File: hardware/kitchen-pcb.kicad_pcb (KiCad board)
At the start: 2 copper layers, 91.6 x 88 mm, 78 parts, among them IC1 ESP32-S3-WROOM-1-N8R8, J1 GSD090012SEU, J2 Conn_02x02_Odd_Even, J3 Conn_01x06, J4 Conn_01x03, J5 DCJ200-10-A-K1-K, J6 USB4105-GF-A, Q1 TEMT6000X01, SW1 SW_Push, SW2 SW_Push, U1 SHT30-DIS-B, U2 MX25L3233FM2I-08G, U3 NCP1117ST33T3G, U4 USBLC6-2SC6

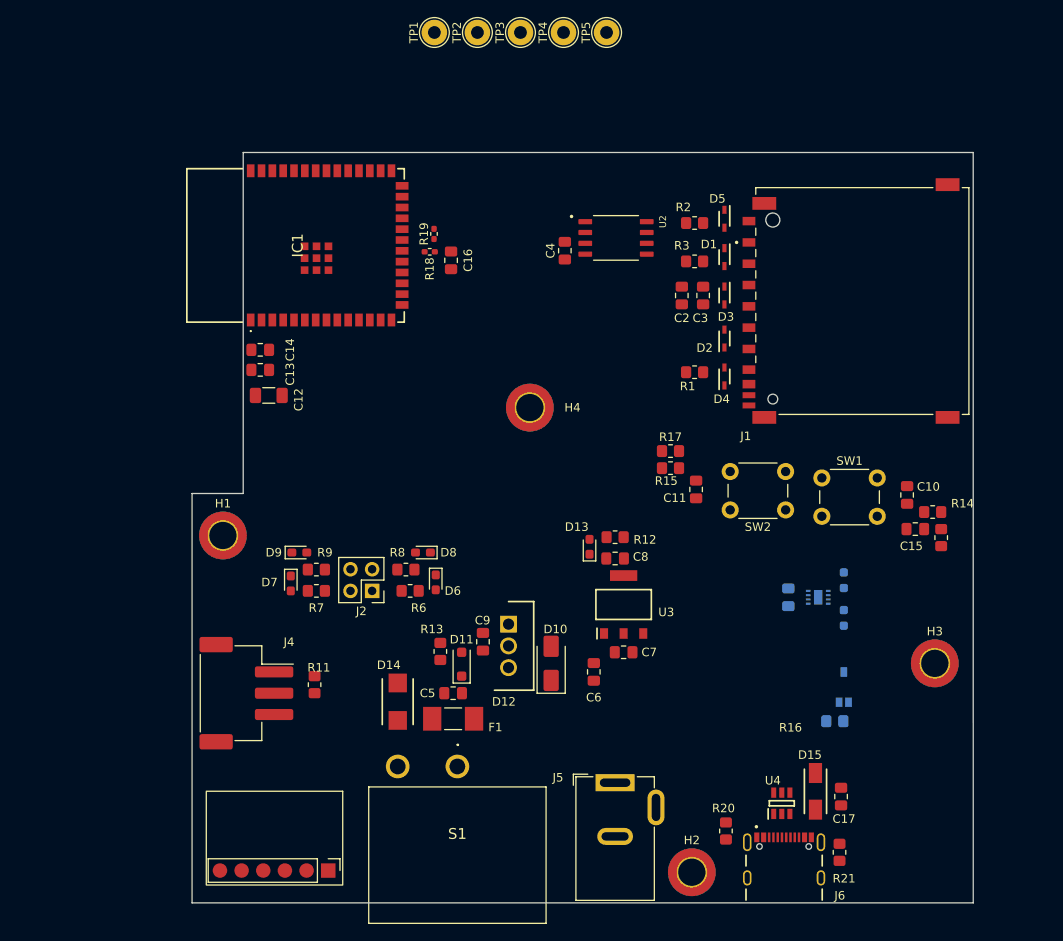
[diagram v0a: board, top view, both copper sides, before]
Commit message: Schematics adjustments - updated some components
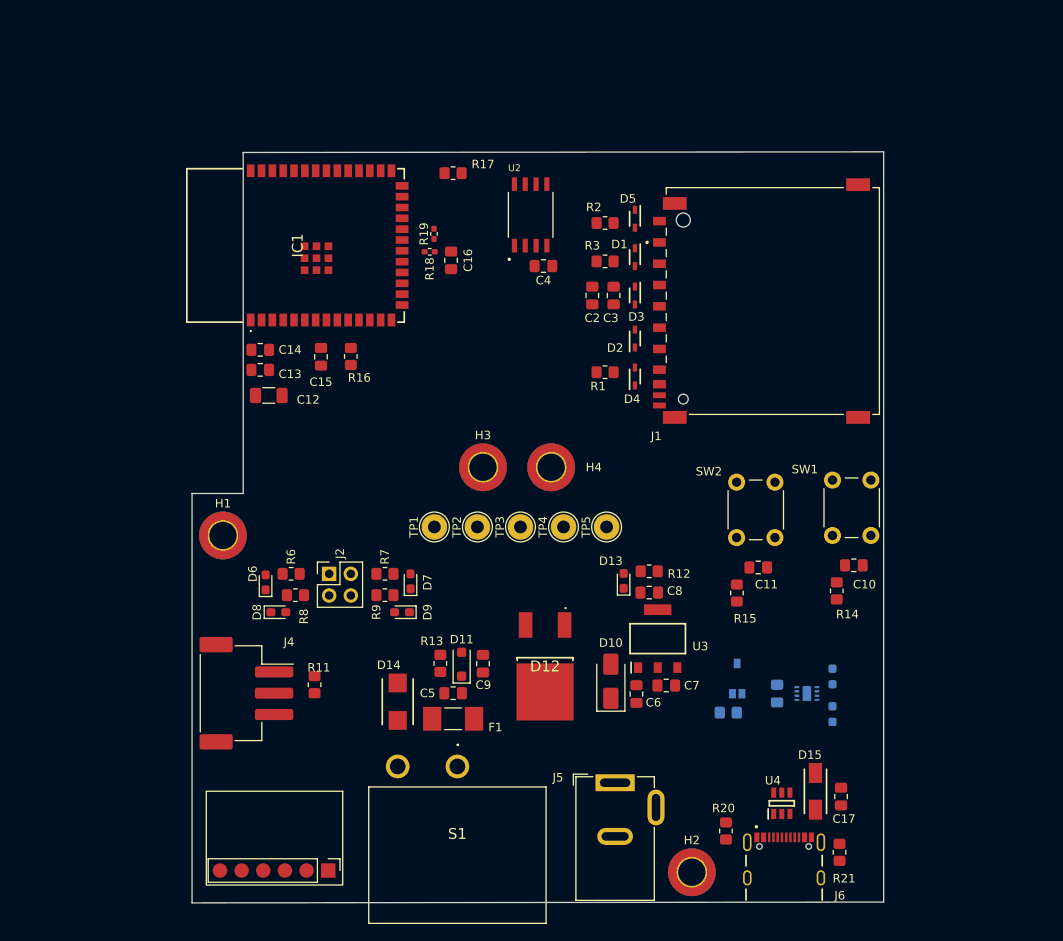
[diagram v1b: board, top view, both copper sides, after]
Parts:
- D11: value NZH6V2B,115 -> NZH5V6B,115
- D12: footprint ESP32-project-footprints:TO255P460X1020X2005-3P -> ESP32-project-footprints:TS820600B
- moved C15 72.6 mm to (112.5, 82.5), turned to 90 degrees
- moved R16 72.4 mm to (116.0, 82.5)
- moved TP1 58.0 mm to (125.8, 102.5)
- moved TP2 58.0 mm to (130.8, 102.5)
- moved TP3 58.0 mm to (135.9, 102.5)
- moved TP4 58.0 mm to (140.9, 102.5)
- moved TP5 58.0 mm to (146.0, 102.5)
- moved H3 57.8 mm to (131.5, 95.5)
- moved R17 41.4 mm to (128.0, 61.0)
- moved D6 20.0 mm to (106.0, 109.0), turned to 90 degrees
- moved D8 18.3 mm to (107.5, 112.5), turned to 0 degrees
- moved R15 16.6 mm to (161.3, 110.2), turned to -90 degrees
- moved R14 14.6 mm to (173.0, 110.0), turned to -90 degrees
- moved R6 14.1 mm to (109.0, 108.0), turned to 180 degrees
- moved D7 14.0 mm to (123.0, 108.9), turned to 90 degrees
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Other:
- board size 91.6 x 88 mm -> 81.1 x 88.1 mm

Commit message: Added notes to schematics, SPI modifications
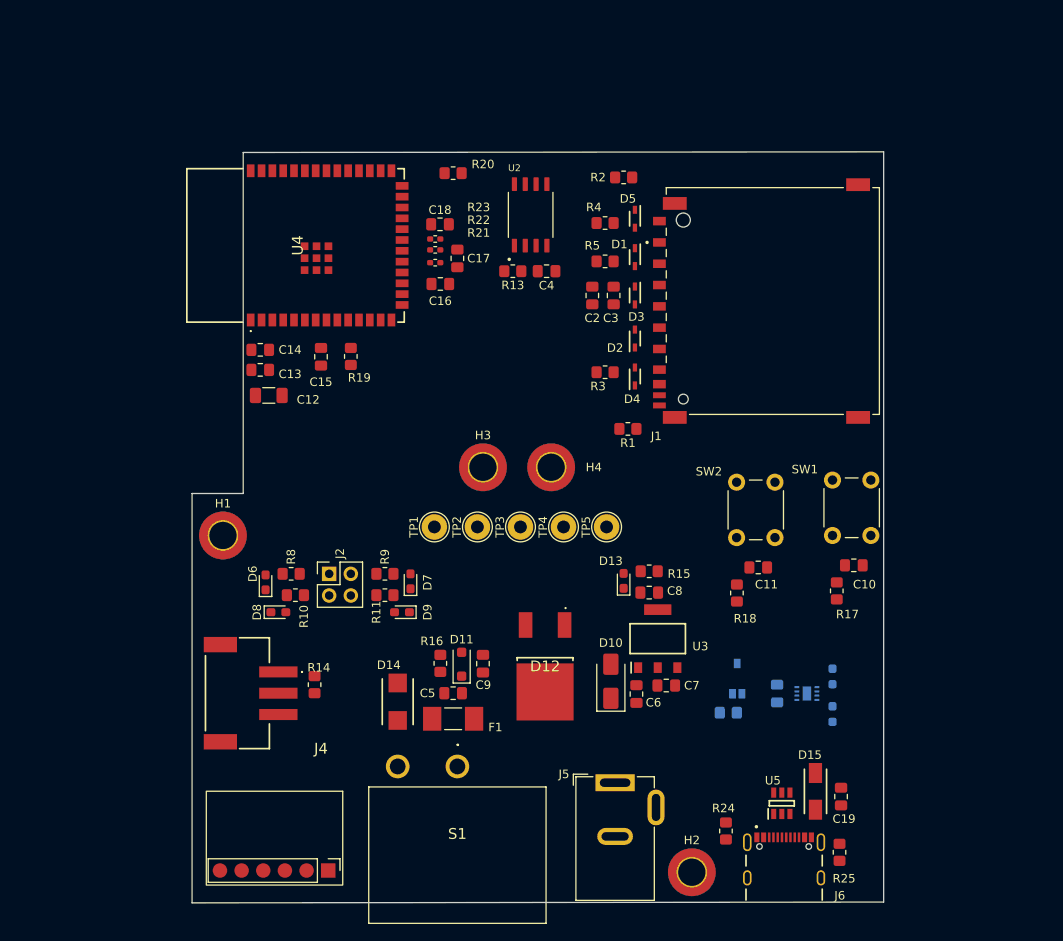
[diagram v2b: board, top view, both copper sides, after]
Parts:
- added C16: 22p, Capacitor_SMD:C_0805_2012Metric_Pad1.18x1.45mm_HandSolder, F.Cu at (126.5, 74.0)
- added C18: 22p, Capacitor_SMD:C_0805_2012Metric_Pad1.18x1.45mm_HandSolder, F.Cu at (126.5, 67.0)
- added R1: 10k, Resistor_SMD:R_0805_2012Metric_Pad1.20x1.40mm_HandSolder, F.Cu at (148.5, 91.0)
- added R13: 10k, Resistor_SMD:R_0805_2012Metric_Pad1.20x1.40mm_HandSolder, F.Cu at (135.0, 72.5)
- added R2: 10k, Resistor_SMD:R_0805_2012Metric_Pad1.20x1.40mm_HandSolder, F.Cu at (148.0, 61.5)
- added R21: 50R, Resistor_SMD:R_0402_1005Metric_Pad0.72x0.64mm_HandSolder, F.Cu at (125.9, 71.5)
- C17: renamed from C16; value 100n -> 22p
- J4: value Conn_01x03 -> S3B-XH-SM4-TB_LF__SN_; footprint Connector_JST:JST_XH_S3B-XH-SM4-TB_1x03-1MP_P2.50mm_Horizontal -> ESP32-project-footprints:S3BXHSM4TBLFSN
- moved C17 0.78 mm to (128.5, 71.0)
- moved C4 0.71 mm to (139.0, 72.5)
- moved R22 0.68 mm to (125.9, 70.0)
- moved R23 0.61 mm to (125.9, 68.7), turned to 0 degrees
- moved J4 0.53 mm to (103.2, 122.0), turned to 90 degrees
- renumbered C17 to C19, R8 to R10, R9 to R11, R10 to R12, R11 to R14, R12 to R15, R13 to R16, R14 to R17, R15 to R18, R16 to R19, R17 to R20, R18 to R22, R19 to R23, R20 to R24, R21 to R25, R1 to R3, R2 to R4, R3 to R5, R4 to R6, R5 to R7, R6 to R8, R7 to R9, IC1 to U4, U4 to U5
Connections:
- J1 pad 8: GND -> Net-(J1-DAT1)
- J1 pad 9: GND -> Net-(J1-DAT2)
- J4 pad 1: +5V -> GND
- J4 pad 3: GND -> +5V
- U2 pad 7: GND -> +3V3
- U4 pad 19: SPI2_MOSI -> Net-(U4-IO11)

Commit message: Layout v0,4
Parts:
- removed H3: MountingHole_Pad, MountingHole:MountingHole_3.2mm_M3_DIN965_Pad_TopBottom
- R21, R22, R23: footprint Resistor_SMD:R_0402_1005Metric_Pad0.72x0.64mm_HandSolder -> Resistor_SMD:R_0603_1608Metric_Pad0.98x0.95mm_HandSolder
- TP1, TP2, TP3, TP4, TP5: footprint TestPoint:TestPoint_THTPad_D3.0mm_Drill1.5mm -> TestPoint:TestPoint_THTPad_D2.0mm_Drill1.0mm
- moved H4 33.6 mm to (137.5, 62.0)
- moved U2 23.6 mm to (124.9, 86.1), turned to 180 degrees
- moved TP5 22.8 mm to (125.5, 92.5), turned to 180 degrees
- moved TP4 21.9 mm to (121.5, 92.5), turned to 180 degrees
- moved D7 21.4 mm to (107.1, 94.5), turned to 0 degrees
- moved J3 20.0 mm to (109.0, 122.0), turned to 0 degrees
- moved D9 19.8 mm to (107.1, 99.5), turned to 0 degrees
- moved D6 17.0 mm to (107.1, 92.0), turned to 0 degrees
- moved R9 16.2 mm to (111.0, 94.5), turned to 180 degrees
- moved R8 16.1 mm to (111.0, 92.0)
- moved R13 16.1 mm to (131.5, 88.2), turned to -90 degrees
- moved D8 15.5 mm to (107.1, 97.0)
- moved R18 14.7 mm to (161.5, 95.5), turned to 180 degrees
- moved SW1 14.4 mm to (174.8, 111.2), turned to 180 degrees
- moved R11 14.2 mm to (111.0, 99.5), turned to 180 degrees
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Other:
- board size 81.1 x 88.1 mm -> 81.1 x 82.5 mm

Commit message: Layout v0.5
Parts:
- moved J5 3.95 mm to (147.0, 127.2)
- moved C19 3.41 mm to (173.4, 128.6)
- moved J6 3.41 mm to (166.8, 138.2)
- moved R24 3.41 mm to (159.9, 132.7)
- moved R25 3.41 mm to (173.2, 135.2)
- moved U5 3.41 mm to (166.5, 129.4)
- moved D15 3.24 mm to (170.4, 127.8)
- moved S1 2.20 mm to (128.5, 123.5)
- moved C14 2.04 mm to (105.6, 83.8)
- moved C15 2.04 mm to (112.7, 84.6)
- moved R19 2.04 mm to (116.2, 84.5)
- moved R21 2.04 mm to (126.1, 73.5)
- moved R22 2.04 mm to (126.1, 72.0)
- moved R23 2.04 mm to (126.1, 70.5)
- moved U4 2.04 mm to (110.0, 71.5)
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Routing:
- added copper zone on F.Cu, net +3V3
- added copper zone on B.Cu, net GND
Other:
- outline, holes or cut-outs redrawn
- board text added: "Devide the board into parts - power - high speed - digital, sensots, ..."
- board text added: "Maybe try to switch MIC MODULE and USBC"
- board text added: "REVISE MISO AND MOSI TERMINATOR RESISTORS PLACEMENT"

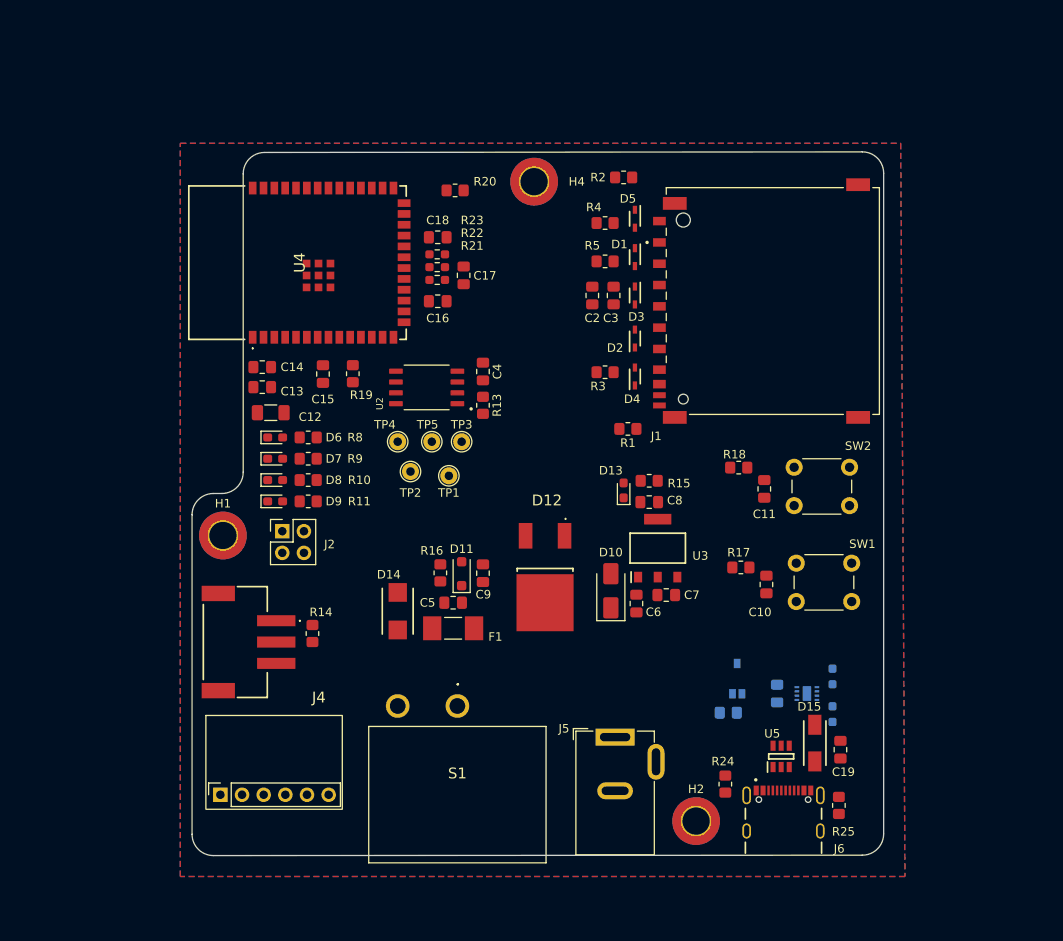
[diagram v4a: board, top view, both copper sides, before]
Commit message: Changed to microSD, layout v0.6.1
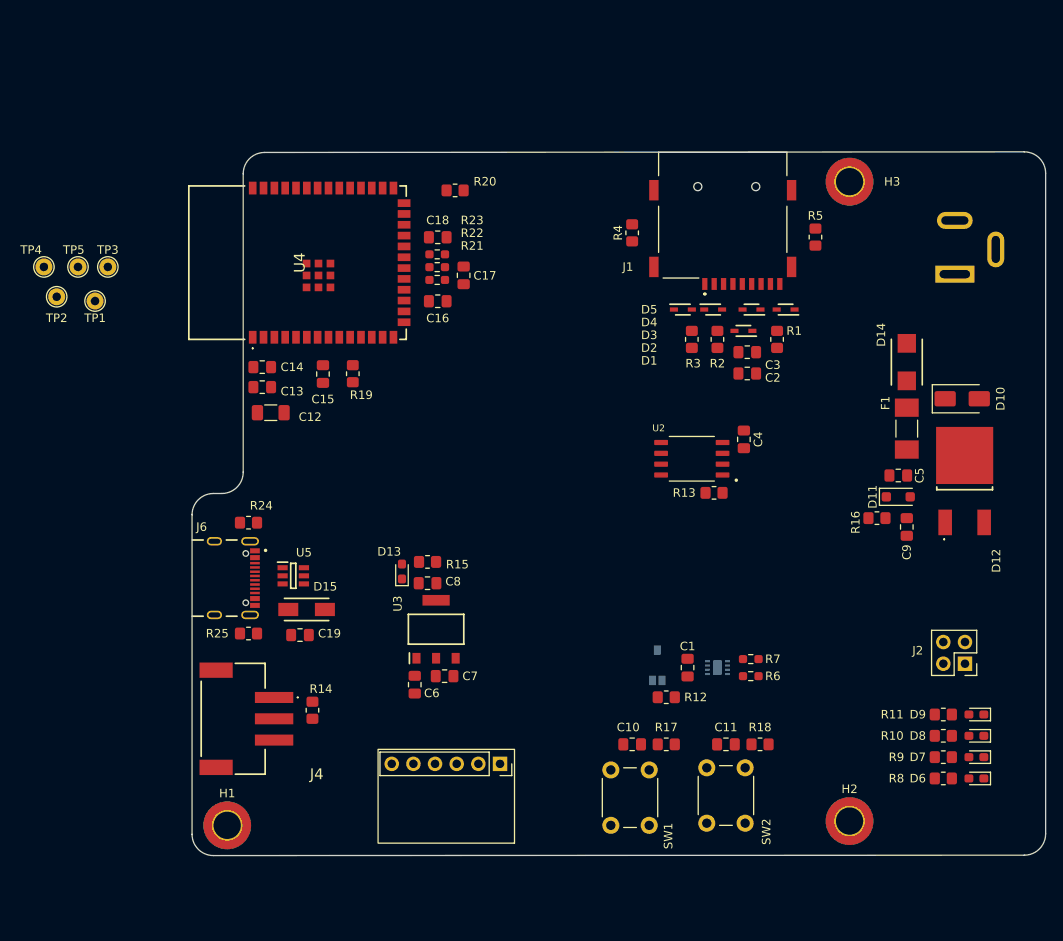
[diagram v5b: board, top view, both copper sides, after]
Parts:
- removed S1: R1966ABLKBLKGR, ESP32-project-footprints:R1966ABLKBLKGR
- C1, R12, R6, R7: moved to F.Cu
- J1: value GSD090012SEU -> MEM2075-00-140-01-A; footprint ESP32-project-footprints:AMPHENOL_GSD090012SEU -> ESP32-project-footprints:MEM20750014001A
- J5: moved to B.Cu
- moved D6 91.5 mm to (189.4, 132.0), turned to 180 degrees
- moved D7 89.4 mm to (189.4, 129.5), turned to 180 degrees
- moved D8 87.6 mm to (189.4, 127.0), turned to 180 degrees
- moved D9 86.0 mm to (189.4, 124.5), turned to 180 degrees
- moved R8 84.6 mm to (185.5, 132.0), turned to 0 degrees
- moved R9 82.3 mm to (185.5, 129.5), turned to 0 degrees
- moved J2 81.6 mm to (188.0, 118.5), turned to 180 degrees
- moved R10 80.3 mm to (185.5, 127.0), turned to 0 degrees
- moved R11 78.6 mm to (185.5, 124.5), turned to 0 degrees
- moved J6 73.0 mm to (100.0, 108.5), turned to -90 degrees
- moved R25 72.1 mm to (104.0, 115.0), turned to 180 degrees
- moved J5 67.4 mm to (186.8, 72.8)
- moved D14 66.5 mm to (181.2, 83.2)
- moved C19 64.8 mm to (110.0, 115.2), turned to 180 degrees
- moved R24 63.8 mm to (104.0, 102.0), turned to 0 degrees
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- renumbered D4 to D1, D1 to D4, H4 to H3, R3 to R1, R5 to R2, R4 to R3, R1 to R4, R2 to R5
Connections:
- J1 pad 1: SPI2_CS_SD -> Net-(J1-DAT2)
- J1 pad 2: SPI2_MOSI -> SPI2_CS_SD
- J1 pad 3: GND -> SPI2_MOSI
- J1 pad 9: Net-(J1-DAT2) -> unconnected-(J1-CD-Pad9)
- R4 pad 1: Net-(J1-DAT1) -> Net-(J1-DAT2)
- R5 pad 1: Net-(J1-DAT2) -> Net-(J1-DAT1)
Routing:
- removed copper zone on F.Cu, net +3V3
- removed copper zone on B.Cu, net GND
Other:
- board size 81.1 x 82.5 mm -> 100.1 x 82.5 mm
- board text removed: "Maybe try to switch MIC MODULE and USBC"

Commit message: Layout v0.6.2, SW1 footprint
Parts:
- added SW1: RA1113112R, ESP32-project-footprints:RA1113112R, B.Cu at (175.2, 93.0)
- moved D6 52.7 mm to (145.6, 102.5), turned to 0 degrees
- moved J2 51.4 mm to (138.5, 105.0), turned to 0 degrees
- moved D7 50.1 mm to (145.6, 105.0), turned to 0 degrees
- moved D8 47.9 mm to (145.6, 107.5), turned to 0 degrees
- moved R8 46.5 mm to (149.5, 102.5), turned to 180 degrees
- moved D9 46.1 mm to (145.6, 110.0), turned to 0 degrees
- moved R9 43.5 mm to (149.5, 105.0), turned to 180 degrees
- moved R10 40.9 mm to (149.5, 107.5), turned to 180 degrees
- moved R11 38.8 mm to (149.5, 110.0), turned to 180 degrees
- moved D14 14.0 mm to (167.5, 86.0), turned to 0 degrees
- moved D12 12.5 mm to (175.5, 97.9)
- moved C5 12.3 mm to (168.0, 98.0)
- moved C9 12.3 mm to (169.0, 104.0)
- moved D11 12.3 mm to (168.0, 100.5)
- moved F1 12.3 mm to (169.0, 92.5)
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- renumbered SW1 to SW2, SW2 to SW3
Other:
- board size 100.1 x 82.5 mm -> 92.6 x 82.5 mm

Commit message: SD card routing v0.1
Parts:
- removed the R21 at (126.1, 73.5)
- added R16: 50R, Resistor_SMD:R_0603_1608Metric_Pad0.98x0.95mm_HandSolder, F.Cu at (145.5, 93.2)
- added R8: 50R, Resistor_SMD:R_0603_1608Metric_Pad0.98x0.95mm_HandSolder, F.Cu at (155.2, 80.5)
- TP1, TP2, TP3, TP4, TP5: footprint TestPoint:TestPoint_THTPad_D2.0mm_Drill1.0mm -> TestPoint:TestPoint_Pad_D2.0mm
- moved J2 36.4 mm to (166.5, 128.2)
- moved H3 26.2 mm to (160.2, 62.0)
- moved D6 23.7 mm to (164.8, 116.4)
- moved D7 23.7 mm to (164.8, 118.9)
- moved D8 23.7 mm to (164.8, 121.4)
- moved D9 23.7 mm to (164.8, 123.9)
- moved R10 23.7 mm to (168.7, 118.9)
- moved R11 23.7 mm to (168.7, 121.4)
- moved R12 23.7 mm to (168.7, 123.9)
- moved R9 23.7 mm to (168.7, 116.4)
- moved C10 21.3 mm to (120.2, 127.8)
- moved C11 21.3 mm to (131.2, 127.8)
- moved R19 21.3 mm to (124.2, 127.8)
- moved R20 21.3 mm to (135.2, 127.8)
- moved SW2 21.3 mm to (117.8, 137.2)
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- renumbered R9 to R10, R10 to R11, R11 to R12, R12 to R13, R13 to R14, R14 to R15, R15 to R17, R16 to R18, R17 to R19, R18 to R20, R19 to R21, R20 to R22, R22 to R24, R24 to R25, R25 to R26, R8 to R9
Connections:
- C19 pad 1: +5V -> /ESP32/VBUS
- D1 pad 2: SPI2_MISO -> Net-(D1-A2)
- J1 pad 7: SPI2_MISO -> Net-(D1-A2)
- R1 pad 1: SPI2_MISO -> Net-(D1-A2)
- R23 pad 1: Net-(U4-IO13) -> Net-(U4-IO11)
- R23 pad 2: SPI2_MISO -> SPI2_MOSI
- U2 pad 2: SPI2_MISO -> Net-(U2-SO/SIO1)
- U4 pad 21: Net-(U4-IO13) -> SPI2_MISO
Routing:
- net +5V: track 0.00 -> 103.6 mm, vias 0 -> 4
- net +3V3: track 0.00 -> 72.3 mm, vias 0 -> 3
- net GND: track 0.00 -> 50.6 mm, vias 0 -> 75
- net SPI2_MISO: track 0.00 -> 41.4 mm, vias 0 -> 2
- net SPI2_CS_SD: track 0.00 -> 39.6 mm, vias 0 -> 2
- net SPI2_MOSI: track 0.00 -> 35.3 mm, vias 0 -> 2
- net /ESP32/USB_D+: track 0.00 -> 31.8 mm
- net /ESP32/USB_D-: track 0.00 -> 31.0 mm
- net SPI2_SCK: track 0.00 -> 29.3 mm, vias 0 -> 2
- net /ESP32/VBUS: track 0.00 -> 23.4 mm, vias 0 -> 3
- net /ESP32/CROWBAR_POWER: track 0.00 -> 20.6 mm
- net Net-(D11-A): track 0.00 -> 15.2 mm
- net Net-(J1-DAT2): track 0.00 -> 12.5 mm
- net /ESP32/CROWBAR_INPUT: track 0.00 -> 9.83 mm
- net /ESP32/DN: track 0.00 -> 9.76 mm
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- added copper zone on F.Cu, net +3V3
- added copper zone on F.Cu, net /ESP32/CROWBAR_POWER
- added copper zone on B.Cu, net GND
- added copper zone on F.Cu, net GND
- added copper zone on In1.Cu, net GND
- added copper zone on In2.Cu, net GND
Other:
- board size 92.6 x 82.5 mm -> 82.6 x 82.5 mm
- copper layers 2 -> 4
- board text added: "ADD TERMINATOR RESISTOR ON EACH MISO LINE NEAR EACH SLAVE"
- board text added: "SPI controlled impedance: https://resources.altium.com/p/there-spi-trace-impedance-requirement"

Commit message: FLASH routing
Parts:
- moved R16 0.15 mm to (145.5, 93.0)
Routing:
- net SPI2_NCS_FLASH: track 0.00 -> 32.3 mm, vias 0 -> 2
- net SPI2_SCK: track 29.3 -> 45.5 mm, vias 2 -> 3
- net SPI2_MISO: track 41.4 -> 57.3 mm
- net +3V3: track 72.3 -> 86.1 mm
- net SPI2_MOSI: track 35.3 -> 47.3 mm, vias 2 -> 3
- net GND: track 50.6 -> 54.2 mm, vias 75 -> 82
- net Net-(U2-SO/SIO1): track 0.00 -> 2.47 mm
- net Net-(D1-A2): track 8.50 -> 9.23 mm
- net /ESP32/USB_D-: track 31.0 -> 31.8 mm
- net (no net): vias 2 -> 0
